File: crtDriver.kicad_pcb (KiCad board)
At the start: 2 copper layers, 79 parts, among them J1 Lum_In, J2 H_Sync, J3 V_Sync, Q1 2N7000, Q10 2N7000, Q11 2N7000, Q12 2N7000, Q13 2N7000, Q14 2N7000, Q15 2N7000, Q16 2N7000, Q17 2N7000, Q2 2N7000, Q3 2N7000, Q4 2N7000, Q5 2N7000, Q6 2N7000, Q7 2N7000, Q8 2N7000, Q9 2N7000, T1 Transformer_1P_1S

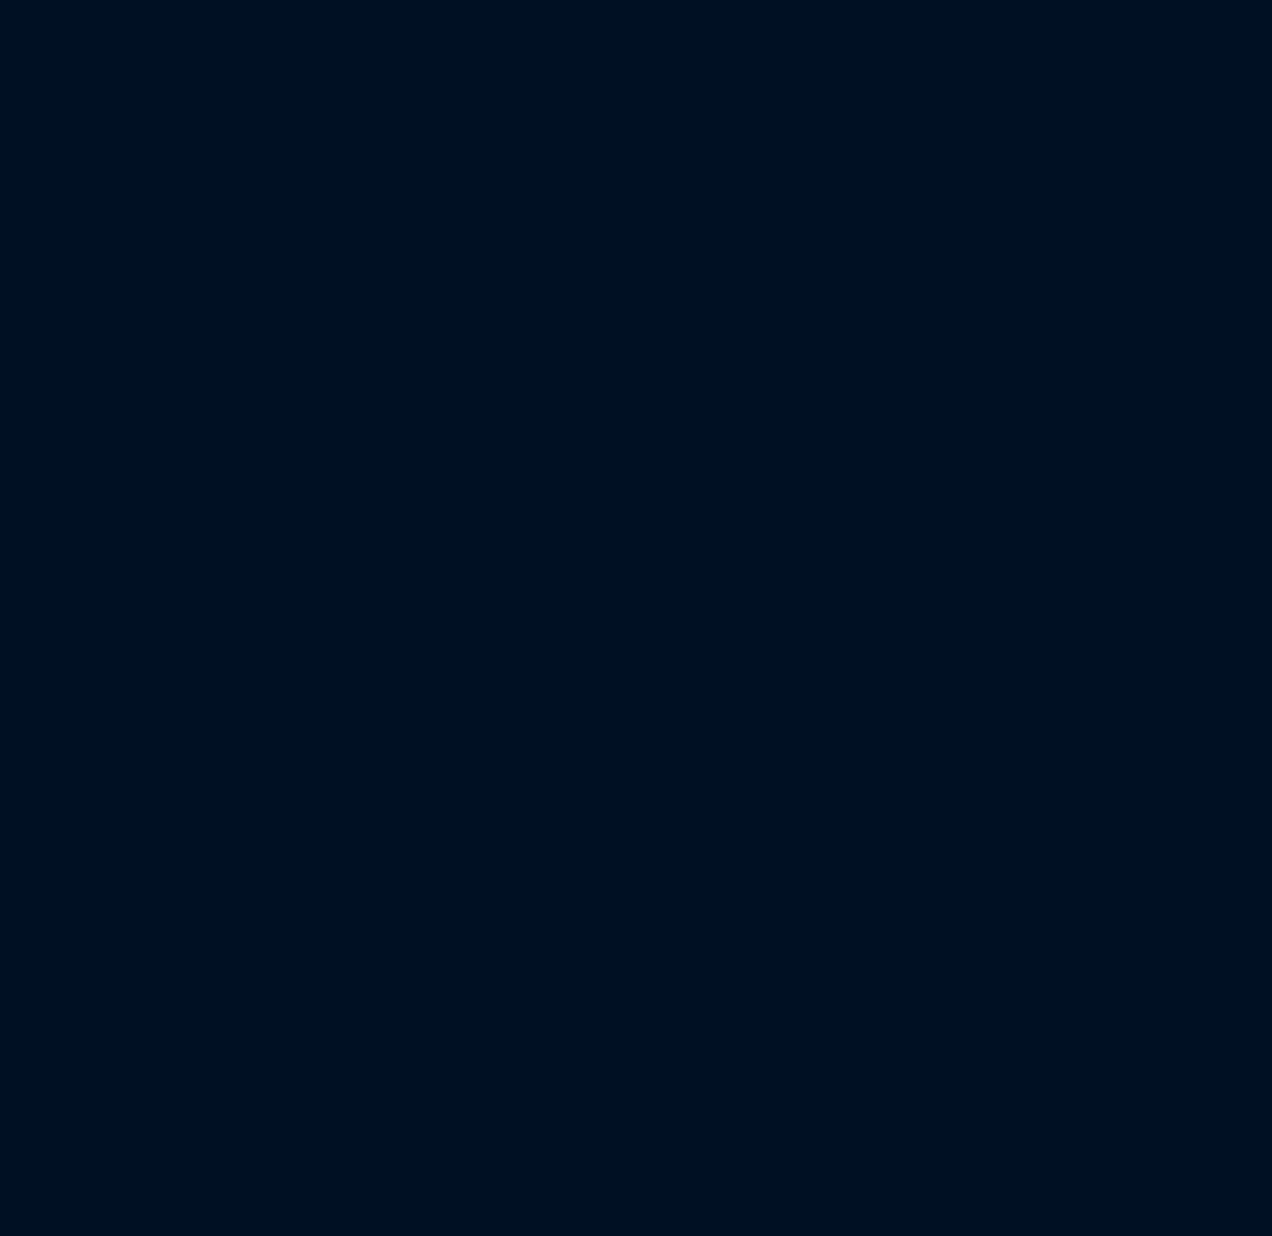
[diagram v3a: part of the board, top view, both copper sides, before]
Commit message: changed bldc driver schematic to use esp32 devkit
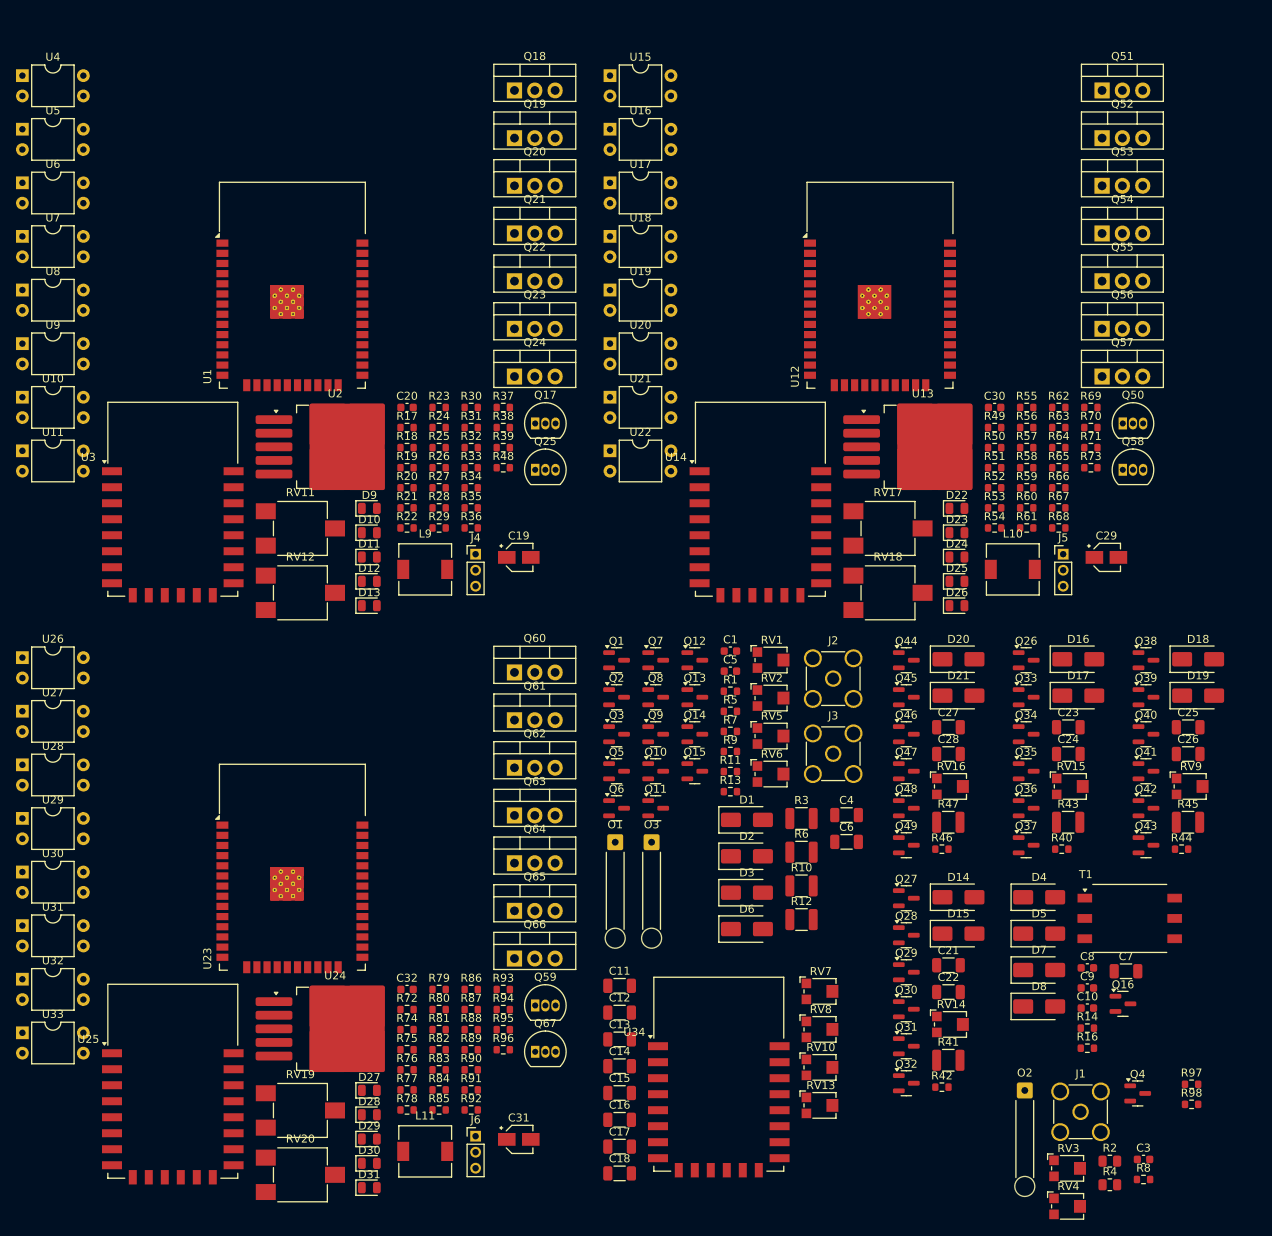
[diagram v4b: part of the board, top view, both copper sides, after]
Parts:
- added C1: 4u, Capacitor_SMD:C_0603_1608Metric, F.Cu at (-22.0, 106.3)
- added C10: 20u, Capacitor_SMD:C_0603_1608Metric, F.Cu at (22.6, 151.0)
- added C11: 40u, Capacitor_SMD:C_1206_3216Metric, F.Cu at (-35.8, 148.2)
- added C12: 40u, Capacitor_SMD:C_1206_3216Metric, F.Cu at (-35.8, 151.5)
- added C13: 40u, Capacitor_SMD:C_1206_3216Metric, F.Cu at (-35.8, 154.9)
- added C14: 40u, Capacitor_SMD:C_1206_3216Metric, F.Cu at (-35.8, 158.2)
- added C15: 40u, Capacitor_SMD:C_1206_3216Metric, F.Cu at (-35.8, 161.6)
- added C16: 40u, Capacitor_SMD:C_1206_3216Metric, F.Cu at (-35.8, 164.9)
- added C17: 40u, Capacitor_SMD:C_1206_3216Metric, F.Cu at (-35.8, 168.3)
- added C18: 40u, Capacitor_SMD:C_1206_3216Metric, F.Cu at (-35.8, 171.6)
- added C19: 470uF 25V, Capacitor_SMD:CP_Elec_3x5.3, F.Cu at (-48.4, 94.6)
- added C20: 4.7uF 25V, Capacitor_SMD:C_0603_1608Metric, F.Cu at (-62.4, 75.9)
- added C21: 47u, Capacitor_SMD:C_1206_3216Metric, F.Cu at (5.29, 145.6)
- added C22: 1u, Capacitor_SMD:C_1206_3216Metric, F.Cu at (5.29, 149.0)
- added C23: 1u, Capacitor_SMD:C_1206_3216Metric, F.Cu at (20.3, 115.9)
- added C24: 47u, Capacitor_SMD:C_1206_3216Metric, F.Cu at (20.3, 119.2)
- added C25: 1u, Capacitor_SMD:C_1206_3216Metric, F.Cu at (35.2, 115.9)
- added C26: 47u, Capacitor_SMD:C_1206_3216Metric, F.Cu at (35.2, 119.2)
- added C27: 1u, Capacitor_SMD:C_1206_3216Metric, F.Cu at (5.29, 115.9)
- added C28: 47u, Capacitor_SMD:C_1206_3216Metric, F.Cu at (5.29, 119.2)
- added C29: 470uF 25V, Capacitor_SMD:CP_Elec_3x5.3, F.Cu at (25.0, 94.6)
- added C3: 100n, Capacitor_SMD:C_0603_1608Metric, F.Cu at (29.7, 169.9)
- added C30: 4.7uF 25V, Capacitor_SMD:C_0603_1608Metric, F.Cu at (11.1, 75.9)
- added C31: 470uF 25V, Capacitor_SMD:CP_Elec_3x5.3, F.Cu at (-48.4, 167.4)
- added C32: 4.7uF 25V, Capacitor_SMD:C_0603_1608Metric, F.Cu at (-62.4, 148.6)
- added C4: 47u, Capacitor_SMD:C_1206_3216Metric, F.Cu at (-7.46, 126.8)
- added C5: 4u, Capacitor_SMD:C_0603_1608Metric, F.Cu at (-22.0, 108.8)
- added C6: 47u, Capacitor_SMD:C_1206_3216Metric, F.Cu at (-7.46, 130.2)
- added C7: 1000u, Capacitor_SMD:C_1206_3216Metric, F.Cu at (27.5, 146.4)
- added C8: 20u, Capacitor_SMD:C_0603_1608Metric, F.Cu at (22.6, 145.9)
- added C9: 20u, Capacitor_SMD:C_0603_1608Metric, F.Cu at (22.6, 148.4)
- added D1: US1A, Diode_SMD:D_SMA, F.Cu at (-19.9, 127.4)
- added D10: 1N4001, Diode_SMD:D_0805_2012Metric, F.Cu at (-67.1, 91.5)
- added D11: 1N4001, Diode_SMD:D_0805_2012Metric, F.Cu at (-67.1, 94.6)
- added D12: 1N4001, Diode_SMD:D_0805_2012Metric, F.Cu at (-67.1, 97.6)
- added D13: 1N4001, Diode_SMD:D_0805_2012Metric, F.Cu at (-67.1, 100.7)
- added D14: US1A, Diode_SMD:D_SMA, F.Cu at (6.53, 137.1)
- added D15: US1A, Diode_SMD:D_SMA, F.Cu at (6.53, 141.7)
- added D16: US1A, Diode_SMD:D_SMA, F.Cu at (21.5, 107.4)
- added D17: US1A, Diode_SMD:D_SMA, F.Cu at (21.5, 111.9)
- added D18: US1A, Diode_SMD:D_SMA, F.Cu at (36.5, 107.4)
- added D19: US1A, Diode_SMD:D_SMA, F.Cu at (36.5, 111.9)
- added D2: US1A, Diode_SMD:D_SMA, F.Cu at (-19.9, 132.0)
- added D20: US1A, Diode_SMD:D_SMA, F.Cu at (6.53, 107.4)
- added D21: US1A, Diode_SMD:D_SMA, F.Cu at (6.53, 111.9)
- added D22: 1N4001, Diode_SMD:D_0805_2012Metric, F.Cu at (6.34, 88.5)
- added D23: 1N4001, Diode_SMD:D_0805_2012Metric, F.Cu at (6.34, 91.5)
- added D24: 1N4001, Diode_SMD:D_0805_2012Metric, F.Cu at (6.34, 94.6)
- added D25: 1N4001, Diode_SMD:D_0805_2012Metric, F.Cu at (6.34, 97.6)
- added D26: 1N4001, Diode_SMD:D_0805_2012Metric, F.Cu at (6.34, 100.7)
- added D27: 1N4001, Diode_SMD:D_0805_2012Metric, F.Cu at (-67.1, 161.3)
- added D28: 1N4001, Diode_SMD:D_0805_2012Metric, F.Cu at (-67.1, 164.3)
- added D29: 1N4001, Diode_SMD:D_0805_2012Metric, F.Cu at (-67.1, 167.3)
- added D3: US1A, Diode_SMD:D_SMA, F.Cu at (-19.9, 136.5)
- added D30: 1N4001, Diode_SMD:D_0805_2012Metric, F.Cu at (-67.1, 170.4)
- added D31: 1N4001, Diode_SMD:D_0805_2012Metric, F.Cu at (-67.1, 173.4)
- added D4: US1A, Diode_SMD:D_SMA, F.Cu at (16.6, 137.1)
- added D5: US1A, Diode_SMD:D_SMA, F.Cu at (16.6, 141.7)
- added D6: US1A, Diode_SMD:D_SMA, F.Cu at (-19.9, 141.1)
- added D7: US1A, Diode_SMD:D_SMA, F.Cu at (16.6, 146.2)
- added D8: US1A, Diode_SMD:D_SMA, F.Cu at (16.6, 150.8)
- added D9: 1N4001, Diode_SMD:D_0805_2012Metric, F.Cu at (-67.1, 88.5)
- added J1: Lum_In, Connector_Coaxial:SMA_Amphenol_901-144_Vertical, F.Cu at (21.8, 163.9)
- added J2: H_Sync, Connector_Coaxial:SMA_Amphenol_901-144_Vertical, F.Cu at (-9.12, 109.8)
- added J3: V_Sync, Connector_Coaxial:SMA_Amphenol_901-144_Vertical, F.Cu at (-9.12, 119.2)
- added J4: Conn_01x03_Female, Connector_PinHeader_2.00mm:PinHeader_1x03_P2.00mm_Vertical, F.Cu at (-53.8, 94.2)
- added J5: Conn_01x03_Female, Connector_PinHeader_2.00mm:PinHeader_1x03_P2.00mm_Vertical, F.Cu at (19.6, 94.2)
- added J6: Conn_01x03_Female, Connector_PinHeader_2.00mm:PinHeader_1x03_P2.00mm_Vertical, F.Cu at (-53.8, 167.0)
- added L10: 9u, Inductor_SMD:L_6.3x6.3_H3, F.Cu at (13.3, 96.1)
- added L11: 9u, Inductor_SMD:L_6.3x6.3_H3, F.Cu at (-60.1, 168.9)
- added L9: 9u, Inductor_SMD:L_6.3x6.3_H3, F.Cu at (-60.1, 96.1)
- added O1: H_Ramp_Out, Connector_Wire:SolderWire-0.25sqmm_1x01_D0.65mm_OD2mm_Relief, F.Cu at (-36.4, 130.2)
- added O2: Lum_Out, Connector_Wire:SolderWire-0.25sqmm_1x01_D0.65mm_OD2mm_Relief, F.Cu at (14.8, 161.3)
- added O3: V_Ramp_Out, Connector_Wire:SolderWire-0.25sqmm_1x01_D0.65mm_OD2mm_Relief, F.Cu at (-31.8, 130.2)
- added Q1: 2N7000, Package_TO_SOT_SMD:SOT-23, F.Cu at (-36.2, 107.5)
- added Q10: 2N7000, Package_TO_SOT_SMD:SOT-23, F.Cu at (-31.3, 121.4)
- added Q11: 2N7000, Package_TO_SOT_SMD:SOT-23, F.Cu at (-31.3, 126.0)
- added Q12: 2N7000, Package_TO_SOT_SMD:SOT-23, F.Cu at (-26.4, 107.5)
- added Q13: 2N7000, Package_TO_SOT_SMD:SOT-23, F.Cu at (-26.4, 112.1)
- added Q14: 2N7000, Package_TO_SOT_SMD:SOT-23, F.Cu at (-26.4, 116.7)
- added Q15: 2N7000, Package_TO_SOT_SMD:SOT-23, F.Cu at (-26.4, 121.4)
- added Q16: 410N, Package_TO_SOT_SMD:SOT-23, F.Cu at (27.1, 150.4)
- added Q17: 2N7000, Package_TO_SOT_THT:TO-92_Inline, F.Cu at (-46.4, 77.9)
- added Q18: IRF3205, Package_TO_SOT_THT:TO-220-3_Vertical, F.Cu at (-49.0, 36.3)
- added Q19: IRF3205, Package_TO_SOT_THT:TO-220-3_Vertical, F.Cu at (-49.0, 42.2)
- added Q2: 2N7000, Package_TO_SOT_SMD:SOT-23, F.Cu at (-36.2, 112.1)
- added Q20: IRF3205, Package_TO_SOT_THT:TO-220-3_Vertical, F.Cu at (-49.0, 48.2)
- added Q21: IRF3205, Package_TO_SOT_THT:TO-220-3_Vertical, F.Cu at (-49.0, 54.1)
- added Q22: IRF3205, Package_TO_SOT_THT:TO-220-3_Vertical, F.Cu at (-49.0, 60.1)
- added Q23: IRF3205, Package_TO_SOT_THT:TO-220-3_Vertical, F.Cu at (-49.0, 66.1)
- added Q24: IRF3205, Package_TO_SOT_THT:TO-220-3_Vertical, F.Cu at (-49.0, 72.0)
- added Q25: 2N7000, Package_TO_SOT_THT:TO-92_Inline, F.Cu at (-46.4, 83.7)
- added Q26: 2N7000, Package_TO_SOT_SMD:SOT-23, F.Cu at (15.0, 107.5)
- added Q27: 2N7000, Package_TO_SOT_SMD:SOT-23, F.Cu at (0.01, 137.2)
- added Q28: 2N7000, Package_TO_SOT_SMD:SOT-23, F.Cu at (0.01, 141.9)
- added Q29: 2N7000, Package_TO_SOT_SMD:SOT-23, F.Cu at (0.01, 146.5)
- added Q3: 2N7000, Package_TO_SOT_SMD:SOT-23, F.Cu at (-36.2, 116.7)
- added Q30: 2N7000, Package_TO_SOT_SMD:SOT-23, F.Cu at (0.01, 151.1)
- added Q31: 2N7000, Package_TO_SOT_SMD:SOT-23, F.Cu at (0.01, 155.7)
- added Q32: 2N7000, Package_TO_SOT_SMD:SOT-23, F.Cu at (0.01, 160.4)
- added Q33: 2N7000, Package_TO_SOT_SMD:SOT-23, F.Cu at (15.0, 112.1)
- added Q34: 2N7000, Package_TO_SOT_SMD:SOT-23, F.Cu at (15.0, 116.7)
- added Q35: 2N7000, Package_TO_SOT_SMD:SOT-23, F.Cu at (15.0, 121.4)
- added Q36: 2N7000, Package_TO_SOT_SMD:SOT-23, F.Cu at (15.0, 126.0)
- added Q37: 2N7000, Package_TO_SOT_SMD:SOT-23, F.Cu at (15.0, 130.6)
- added Q38: 2N7000, Package_TO_SOT_SMD:SOT-23, F.Cu at (30.0, 107.5)
- added Q39: 2N7000, Package_TO_SOT_SMD:SOT-23, F.Cu at (30.0, 112.1)
- added Q4: 2N7000, Package_TO_SOT_SMD:SOT-23, F.Cu at (28.9, 161.6)
- added Q40: 2N7000, Package_TO_SOT_SMD:SOT-23, F.Cu at (30.0, 116.7)
- added Q41: 2N7000, Package_TO_SOT_SMD:SOT-23, F.Cu at (30.0, 121.4)
- added Q42: 2N7000, Package_TO_SOT_SMD:SOT-23, F.Cu at (30.0, 126.0)
- added Q43: 2N7000, Package_TO_SOT_SMD:SOT-23, F.Cu at (30.0, 130.6)
- added Q44: 2N7000, Package_TO_SOT_SMD:SOT-23, F.Cu at (0.01, 107.5)
- added Q45: 2N7000, Package_TO_SOT_SMD:SOT-23, F.Cu at (0.01, 112.1)
- added Q46: 2N7000, Package_TO_SOT_SMD:SOT-23, F.Cu at (0.01, 116.7)
- added Q47: 2N7000, Package_TO_SOT_SMD:SOT-23, F.Cu at (0.01, 121.4)
- added Q48: 2N7000, Package_TO_SOT_SMD:SOT-23, F.Cu at (0.01, 126.0)
- added Q49: 2N7000, Package_TO_SOT_SMD:SOT-23, F.Cu at (0.01, 130.6)
- added Q5: 2N7000, Package_TO_SOT_SMD:SOT-23, F.Cu at (-36.2, 121.4)
- added Q50: 2N7000, Package_TO_SOT_THT:TO-92_Inline, F.Cu at (27.1, 77.9)
- added Q51: IRF3205, Package_TO_SOT_THT:TO-220-3_Vertical, F.Cu at (24.5, 36.3)
- added Q52: IRF3205, Package_TO_SOT_THT:TO-220-3_Vertical, F.Cu at (24.5, 42.2)
- added Q53: IRF3205, Package_TO_SOT_THT:TO-220-3_Vertical, F.Cu at (24.5, 48.2)
- added Q54: IRF3205, Package_TO_SOT_THT:TO-220-3_Vertical, F.Cu at (24.5, 54.1)
- added Q55: IRF3205, Package_TO_SOT_THT:TO-220-3_Vertical, F.Cu at (24.5, 60.1)
- added Q56: IRF3205, Package_TO_SOT_THT:TO-220-3_Vertical, F.Cu at (24.5, 66.1)
- added Q57: IRF3205, Package_TO_SOT_THT:TO-220-3_Vertical, F.Cu at (24.5, 72.0)
- added Q58: 2N7000, Package_TO_SOT_THT:TO-92_Inline, F.Cu at (27.1, 83.7)
- added Q59: 2N7000, Package_TO_SOT_THT:TO-92_Inline, F.Cu at (-46.4, 150.6)
- added Q6: 2N7000, Package_TO_SOT_SMD:SOT-23, F.Cu at (-36.2, 126.0)
- added Q60: IRF3205, Package_TO_SOT_THT:TO-220-3_Vertical, F.Cu at (-49.0, 109.0)
- added Q61: IRF3205, Package_TO_SOT_THT:TO-220-3_Vertical, F.Cu at (-49.0, 115.0)
- added Q62: IRF3205, Package_TO_SOT_THT:TO-220-3_Vertical, F.Cu at (-49.0, 120.9)
- added Q63: IRF3205, Package_TO_SOT_THT:TO-220-3_Vertical, F.Cu at (-49.0, 126.9)
- added Q64: IRF3205, Package_TO_SOT_THT:TO-220-3_Vertical, F.Cu at (-49.0, 132.8)
- added Q65: IRF3205, Package_TO_SOT_THT:TO-220-3_Vertical, F.Cu at (-49.0, 138.8)
- added Q66: IRF3205, Package_TO_SOT_THT:TO-220-3_Vertical, F.Cu at (-49.0, 144.8)
- added Q67: 2N7000, Package_TO_SOT_THT:TO-92_Inline, F.Cu at (-46.4, 156.4)
- added Q7: 2N7000, Package_TO_SOT_SMD:SOT-23, F.Cu at (-31.3, 107.5)
- added Q8: 2N7000, Package_TO_SOT_SMD:SOT-23, F.Cu at (-31.3, 112.1)
- added Q9: 2N7000, Package_TO_SOT_SMD:SOT-23, F.Cu at (-31.3, 116.7)
- added R1: 1000000, Resistor_SMD:R_0603_1608Metric, F.Cu at (-22.0, 111.4)
- added R10: 1000, Resistor_SMD:R_1210_3225Metric, F.Cu at (-13.1, 135.7)
- added R11: 10000, Resistor_SMD:R_0603_1608Metric, F.Cu at (-22.0, 121.4)
- added R12: 10, Resistor_SMD:R_1210_3225Metric, F.Cu at (-13.1, 139.9)
- added R13: 1000, Resistor_SMD:R_0603_1608Metric, F.Cu at (-22.0, 123.9)
- added R14: 4, Resistor_SMD:R_0603_1608Metric, F.Cu at (22.6, 153.5)
- added R16: 100000, Resistor_SMD:R_0603_1608Metric, F.Cu at (22.6, 156.0)
- added R17: 1K, Resistor_SMD:R_0603_1608Metric, F.Cu at (-62.4, 78.4)
- added R18: 200, Resistor_SMD:R_0603_1608Metric, F.Cu at (-62.4, 80.9)
- added R19: 200, Resistor_SMD:R_0603_1608Metric, F.Cu at (-62.4, 83.4)
- added R2: 100000, Resistor_SMD:R_0805_2012Metric, F.Cu at (25.5, 170.1)
- added R20: 200, Resistor_SMD:R_0603_1608Metric, F.Cu at (-62.4, 85.9)
- added R21: 200, Resistor_SMD:R_0603_1608Metric, F.Cu at (-62.4, 88.4)
- added R22: 200, Resistor_SMD:R_0603_1608Metric, F.Cu at (-62.4, 91.0)
- added R23: 200, Resistor_SMD:R_0603_1608Metric, F.Cu at (-58.4, 75.9)
- added R24: 1K, Resistor_SMD:R_0603_1608Metric, F.Cu at (-58.4, 78.4)
- added R25: 10K, Resistor_SMD:R_0603_1608Metric, F.Cu at (-58.4, 80.9)
- added R26: 1K, Resistor_SMD:R_0603_1608Metric, F.Cu at (-58.4, 83.4)
- added R27: 1K, Resistor_SMD:R_0603_1608Metric, F.Cu at (-58.4, 85.9)
- added R28: 1K, Resistor_SMD:R_0603_1608Metric, F.Cu at (-58.4, 88.4)
- added R29: 1K, Resistor_SMD:R_0603_1608Metric, F.Cu at (-58.4, 91.0)
- added R3: 1000, Resistor_SMD:R_1210_3225Metric, F.Cu at (-13.1, 127.3)
- added R30: 1K, Resistor_SMD:R_0603_1608Metric, F.Cu at (-54.4, 75.9)
- added R31: 10K, Resistor_SMD:R_0603_1608Metric, F.Cu at (-54.4, 78.4)
- added R32: 10K, Resistor_SMD:R_0603_1608Metric, F.Cu at (-54.4, 80.9)
- added R33: 10K, Resistor_SMD:R_0603_1608Metric, F.Cu at (-54.4, 83.4)
- added R34: 10K, Resistor_SMD:R_0603_1608Metric, F.Cu at (-54.4, 85.9)
- added R35: 10K, Resistor_SMD:R_0603_1608Metric, F.Cu at (-54.4, 88.4)
- added R36: 10K, Resistor_SMD:R_0603_1608Metric, F.Cu at (-54.4, 91.0)
- added R37: 10K, Resistor_SMD:R_0603_1608Metric, F.Cu at (-50.4, 75.9)
- added R38: 10K, Resistor_SMD:R_0603_1608Metric, F.Cu at (-50.4, 78.4)
- added R39: 1K, Resistor_SMD:R_0603_1608Metric, F.Cu at (-50.4, 80.9)
- added R4: 100, Resistor_SMD:R_0805_2012Metric, F.Cu at (25.5, 173.1)
- added R40: 10000, Resistor_SMD:R_0603_1608Metric, F.Cu at (19.4, 131.1)
- added R41: 10, Resistor_SMD:R_1210_3225Metric, F.Cu at (5.26, 157.5)
- added R42: 10000, Resistor_SMD:R_0603_1608Metric, F.Cu at (4.46, 160.8)
- added R43: 10, Resistor_SMD:R_1210_3225Metric, F.Cu at (20.2, 127.7)
- added R44: 10000, Resistor_SMD:R_0603_1608Metric, F.Cu at (34.4, 131.1)
- added R45: 10, Resistor_SMD:R_1210_3225Metric, F.Cu at (35.2, 127.7)
- added R46: 10000, Resistor_SMD:R_0603_1608Metric, F.Cu at (4.46, 131.1)
- added R47: 10, Resistor_SMD:R_1210_3225Metric, F.Cu at (5.26, 127.7)
- added R48: 0, Resistor_SMD:R_0603_1608Metric, F.Cu at (-50.4, 83.4)
- added R49: 1K, Resistor_SMD:R_0603_1608Metric, F.Cu at (11.1, 78.4)
- added R5: 10000, Resistor_SMD:R_0603_1608Metric, F.Cu at (-22.0, 113.9)
- added R50: 200, Resistor_SMD:R_0603_1608Metric, F.Cu at (11.1, 80.9)
- added R51: 200, Resistor_SMD:R_0603_1608Metric, F.Cu at (11.1, 83.4)
- added R52: 200, Resistor_SMD:R_0603_1608Metric, F.Cu at (11.1, 85.9)
- added R53: 200, Resistor_SMD:R_0603_1608Metric, F.Cu at (11.1, 88.4)
- added R54: 200, Resistor_SMD:R_0603_1608Metric, F.Cu at (11.1, 91.0)
- added R55: 200, Resistor_SMD:R_0603_1608Metric, F.Cu at (15.1, 75.9)
- added R56: 1K, Resistor_SMD:R_0603_1608Metric, F.Cu at (15.1, 78.4)
- added R57: 10K, Resistor_SMD:R_0603_1608Metric, F.Cu at (15.1, 80.9)
- added R58: 1K, Resistor_SMD:R_0603_1608Metric, F.Cu at (15.1, 83.4)
- added R59: 1K, Resistor_SMD:R_0603_1608Metric, F.Cu at (15.1, 85.9)
- added R6: 10, Resistor_SMD:R_1210_3225Metric, F.Cu at (-13.1, 131.5)
- added R60: 1K, Resistor_SMD:R_0603_1608Metric, F.Cu at (15.1, 88.4)
- added R61: 1K, Resistor_SMD:R_0603_1608Metric, F.Cu at (15.1, 91.0)
- added R62: 1K, Resistor_SMD:R_0603_1608Metric, F.Cu at (19.1, 75.9)
- added R63: 10K, Resistor_SMD:R_0603_1608Metric, F.Cu at (19.1, 78.4)
- added R64: 10K, Resistor_SMD:R_0603_1608Metric, F.Cu at (19.1, 80.9)
- added R65: 10K, Resistor_SMD:R_0603_1608Metric, F.Cu at (19.1, 83.4)
- added R66: 10K, Resistor_SMD:R_0603_1608Metric, F.Cu at (19.1, 85.9)
- added R67: 10K, Resistor_SMD:R_0603_1608Metric, F.Cu at (19.1, 88.4)
- added R68: 10K, Resistor_SMD:R_0603_1608Metric, F.Cu at (19.1, 91.0)
- added R69: 10K, Resistor_SMD:R_0603_1608Metric, F.Cu at (23.1, 75.9)
- added R7: 1000, Resistor_SMD:R_0603_1608Metric, F.Cu at (-22.0, 116.4)
- added R70: 10K, Resistor_SMD:R_0603_1608Metric, F.Cu at (23.1, 78.4)
- added R71: 1K, Resistor_SMD:R_0603_1608Metric, F.Cu at (23.1, 80.9)
- added R72: 0, Resistor_SMD:R_0603_1608Metric, F.Cu at (-62.4, 151.2)
- added R73: 0, Resistor_SMD:R_0603_1608Metric, F.Cu at (23.1, 83.4)
- added R74: 1K, Resistor_SMD:R_0603_1608Metric, F.Cu at (-62.4, 153.7)
- added R75: 200, Resistor_SMD:R_0603_1608Metric, F.Cu at (-62.4, 156.2)
- added R76: 200, Resistor_SMD:R_0603_1608Metric, F.Cu at (-62.4, 158.7)
- added R77: 200, Resistor_SMD:R_0603_1608Metric, F.Cu at (-62.4, 161.2)
- added R78: 200, Resistor_SMD:R_0603_1608Metric, F.Cu at (-62.4, 163.7)
- added R79: 200, Resistor_SMD:R_0603_1608Metric, F.Cu at (-58.4, 148.6)
- added R8: 10000, Resistor_SMD:R_0603_1608Metric, F.Cu at (29.7, 172.4)
- added R80: 200, Resistor_SMD:R_0603_1608Metric, F.Cu at (-58.4, 151.2)
- added R81: 1K, Resistor_SMD:R_0603_1608Metric, F.Cu at (-58.4, 153.7)
- added R82: 10K, Resistor_SMD:R_0603_1608Metric, F.Cu at (-58.4, 156.2)
- added R83: 1K, Resistor_SMD:R_0603_1608Metric, F.Cu at (-58.4, 158.7)
- added R84: 1K, Resistor_SMD:R_0603_1608Metric, F.Cu at (-58.4, 161.2)
- added R85: 1K, Resistor_SMD:R_0603_1608Metric, F.Cu at (-58.4, 163.7)
- added R86: 1K, Resistor_SMD:R_0603_1608Metric, F.Cu at (-54.4, 148.6)
- added R87: 1K, Resistor_SMD:R_0603_1608Metric, F.Cu at (-54.4, 151.2)
- added R88: 10K, Resistor_SMD:R_0603_1608Metric, F.Cu at (-54.4, 153.7)
- added R89: 10K, Resistor_SMD:R_0603_1608Metric, F.Cu at (-54.4, 156.2)
- added R9: 1000000, Resistor_SMD:R_0603_1608Metric, F.Cu at (-22.0, 118.9)
- added R90: 10K, Resistor_SMD:R_0603_1608Metric, F.Cu at (-54.4, 158.7)
- added R91: 10K, Resistor_SMD:R_0603_1608Metric, F.Cu at (-54.4, 161.2)
- added R92: 10K, Resistor_SMD:R_0603_1608Metric, F.Cu at (-54.4, 163.7)
- added R93: 10K, Resistor_SMD:R_0603_1608Metric, F.Cu at (-50.4, 148.6)
- added R94: 10K, Resistor_SMD:R_0603_1608Metric, F.Cu at (-50.4, 151.2)
- added R95: 10K, Resistor_SMD:R_0603_1608Metric, F.Cu at (-50.4, 153.7)
- added R96: 1K, Resistor_SMD:R_0603_1608Metric, F.Cu at (-50.4, 156.2)
- added R97: 4.7K, Resistor_SMD:R_0603_1608Metric, F.Cu at (35.7, 160.5)
- added R98: 4.7K, Resistor_SMD:R_0603_1608Metric, F.Cu at (35.7, 163.0)
- added RV1: 2M, Potentiometer_SMD:Potentiometer_Bourns_TC33X_Vertical, F.Cu at (-16.8, 107.5)
- added RV10: 2M, Potentiometer_SMD:Potentiometer_Bourns_TC33X_Vertical, F.Cu at (-10.7, 158.4)
- added RV11: 50K POT, Potentiometer_SMD:Potentiometer_ACP_CA6-VSMD_Vertical, F.Cu at (-75.7, 91.0)
- added RV12: 2K POT, Potentiometer_SMD:Potentiometer_ACP_CA6-VSMD_Vertical, F.Cu at (-75.7, 99.1)
- added RV13: 2M, Potentiometer_SMD:Potentiometer_Bourns_TC33X_Vertical, F.Cu at (-10.7, 163.1)
- added RV14: 250, Potentiometer_SMD:Potentiometer_Bourns_TC33X_Vertical, F.Cu at (5.63, 153.0)
- added RV15: 250, Potentiometer_SMD:Potentiometer_Bourns_TC33X_Vertical, F.Cu at (20.6, 123.3)
- added RV16: 250, Potentiometer_SMD:Potentiometer_Bourns_TC33X_Vertical, F.Cu at (5.63, 123.3)
- added RV17: 50K POT, Potentiometer_SMD:Potentiometer_ACP_CA6-VSMD_Vertical, F.Cu at (-2.27, 91.0)
- added RV18: 2K POT, Potentiometer_SMD:Potentiometer_ACP_CA6-VSMD_Vertical, F.Cu at (-2.27, 99.1)
- added RV19: 50K POT, Potentiometer_SMD:Potentiometer_ACP_CA6-VSMD_Vertical, F.Cu at (-75.7, 163.8)
- added RV2: 250, Potentiometer_SMD:Potentiometer_Bourns_TC33X_Vertical, F.Cu at (-16.8, 112.2)
- added RV20: 2K POT, Potentiometer_SMD:Potentiometer_ACP_CA6-VSMD_Vertical, F.Cu at (-75.7, 171.8)
- added RV3: 2M, Potentiometer_SMD:Potentiometer_Bourns_TC33X_Vertical, F.Cu at (20.3, 171.0)
- added RV4: 2000, Potentiometer_SMD:Potentiometer_Bourns_TC33X_Vertical, F.Cu at (20.3, 175.8)
- added RV5: 2M, Potentiometer_SMD:Potentiometer_Bourns_TC33X_Vertical, F.Cu at (-16.8, 117.0)
- added RV6: 5000, Potentiometer_SMD:Potentiometer_Bourns_TC33X_Vertical, F.Cu at (-16.8, 121.7)
- added RV7: 2M, Potentiometer_SMD:Potentiometer_Bourns_TC33X_Vertical, F.Cu at (-10.7, 148.9)
- added RV8: 2M, Potentiometer_SMD:Potentiometer_Bourns_TC33X_Vertical, F.Cu at (-10.7, 153.6)
- added RV9: 250, Potentiometer_SMD:Potentiometer_Bourns_TC33X_Vertical, F.Cu at (35.6, 123.3)
- added T1: Wuerth_750315371, Transformer_SMD:Transformer_Wuerth_750315371, F.Cu at (27.9, 139.8)
- added U1: ESP32-WROOM-32, RF_Module:ESP32-WROOM-32, F.Cu at (-76.7, 63.6)
- added U10: PC817, Package_DIP:DIP-4_W7.62mm, F.Cu at (-110.5, 74.6)
- added U11: PC817, Package_DIP:DIP-4_W7.62mm, F.Cu at (-110.5, 81.3)
- added U12: ESP32-WROOM-32, RF_Module:ESP32-WROOM-32, F.Cu at (-3.27, 63.6)
- added U13: LM2576HVS-5, Package_TO_SOT_SMD:TO-263-5_TabPin3, F.Cu at (2.08, 80.8)
- added U14: ESP-12E, RF_Module:ESP-12E, F.Cu at (-18.2, 87.4)
- added U15: PC817, Package_DIP:DIP-4_W7.62mm, F.Cu at (-37.0, 34.4)
- added U16: PC817, Package_DIP:DIP-4_W7.62mm, F.Cu at (-37.0, 41.1)
- added U17: PC817, Package_DIP:DIP-4_W7.62mm, F.Cu at (-37.0, 47.8)
- added U18: PC817, Package_DIP:DIP-4_W7.62mm, F.Cu at (-37.0, 54.5)
- added U19: PC817, Package_DIP:DIP-4_W7.62mm, F.Cu at (-37.0, 61.2)
- added U2: LM2576HVS-5, Package_TO_SOT_SMD:TO-263-5_TabPin3, F.Cu at (-71.4, 80.8)
- added U20: PC817, Package_DIP:DIP-4_W7.62mm, F.Cu at (-37.0, 67.9)
- added U21: PC817, Package_DIP:DIP-4_W7.62mm, F.Cu at (-37.0, 74.6)
- added U22: PC817, Package_DIP:DIP-4_W7.62mm, F.Cu at (-37.0, 81.3)
- added U23: ESP32-WROOM-32, RF_Module:ESP32-WROOM-32, F.Cu at (-76.7, 136.3)
- added U24: LM2576HVS-5, Package_TO_SOT_SMD:TO-263-5_TabPin3, F.Cu at (-71.4, 153.6)
- added U25: ESP-12E, RF_Module:ESP-12E, F.Cu at (-91.7, 160.1)
- added U26: PC817, Package_DIP:DIP-4_W7.62mm, F.Cu at (-110.5, 107.2)
- added U27: PC817, Package_DIP:DIP-4_W7.62mm, F.Cu at (-110.5, 113.9)
- added U28: PC817, Package_DIP:DIP-4_W7.62mm, F.Cu at (-110.5, 120.6)
- added U29: PC817, Package_DIP:DIP-4_W7.62mm, F.Cu at (-110.5, 127.3)
- added U3: ESP-12E, RF_Module:ESP-12E, F.Cu at (-91.7, 87.4)
- added U30: PC817, Package_DIP:DIP-4_W7.62mm, F.Cu at (-110.5, 134.0)
- added U31: PC817, Package_DIP:DIP-4_W7.62mm, F.Cu at (-110.5, 140.7)
- added U32: PC817, Package_DIP:DIP-4_W7.62mm, F.Cu at (-110.5, 147.4)
- added U33: PC817, Package_DIP:DIP-4_W7.62mm, F.Cu at (-110.5, 154.1)
- added U34: ESP-12E, RF_Module:ESP-12E, F.Cu at (-23.4, 159.2)
- added U4: PC817, Package_DIP:DIP-4_W7.62mm, F.Cu at (-110.5, 34.4)
- added U5: PC817, Package_DIP:DIP-4_W7.62mm, F.Cu at (-110.5, 41.1)
- added U6: PC817, Package_DIP:DIP-4_W7.62mm, F.Cu at (-110.5, 47.8)
- added U7: PC817, Package_DIP:DIP-4_W7.62mm, F.Cu at (-110.5, 54.5)
- added U8: PC817, Package_DIP:DIP-4_W7.62mm, F.Cu at (-110.5, 61.2)
- added U9: PC817, Package_DIP:DIP-4_W7.62mm, F.Cu at (-110.5, 67.9)
- C2: value 500u -> 2000u
